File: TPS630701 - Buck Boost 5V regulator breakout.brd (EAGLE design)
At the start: 29.2 x 17.5 mm, 17 parts, among them IC1 TPS630701RNMT

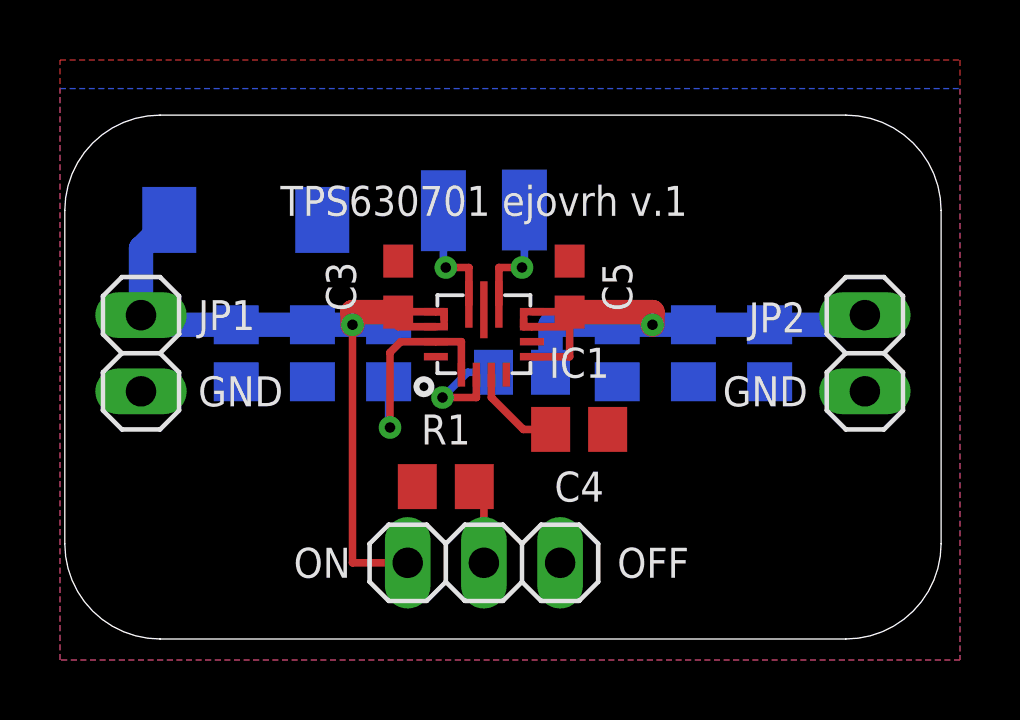
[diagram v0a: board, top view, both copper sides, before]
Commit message: - recreated gerbers with better layer names & corrected mission dimension layer
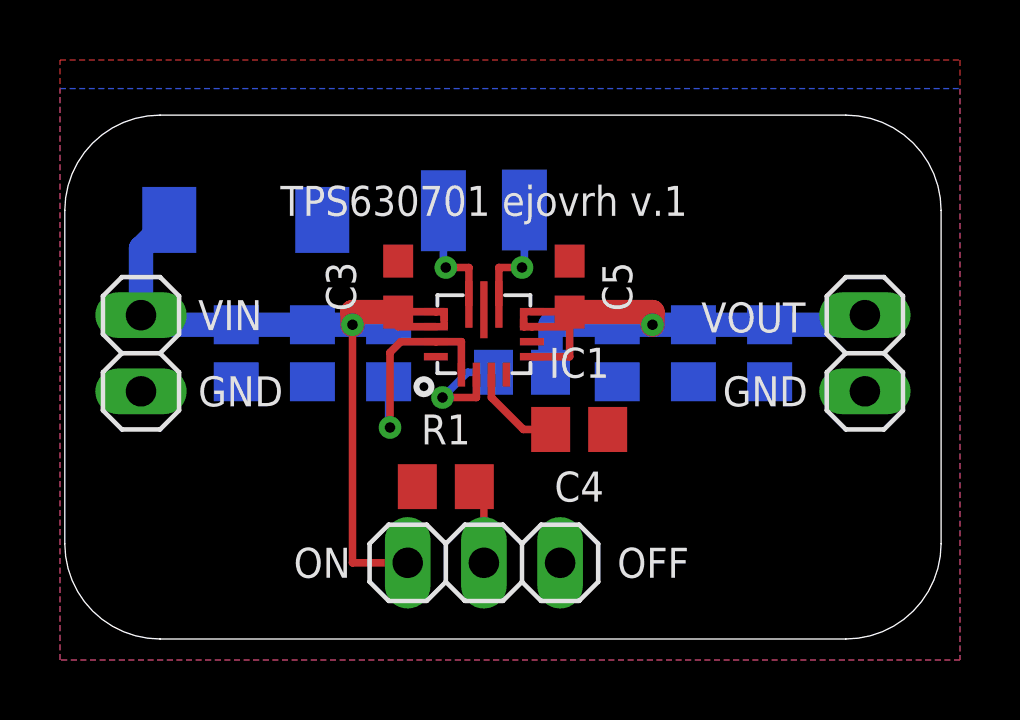
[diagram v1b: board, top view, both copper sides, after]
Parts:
- renumbered JP1 to VIN, JP2 to VOUT
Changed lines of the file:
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@@
 <layer number="14" name="Route14" color="1" fill="6" visible="no" active="no"/>
 <layer number="15" name="Route15" color="4" fill="6" visible="no" active="no"/>
-<layer number="16" name="Bottom" color="1" fill="1" visible="no" active="yes"/>
+<layer number="16" name="Bottom" color="1" fill="1" visible="yes" active="yes"/>
 <layer number="17" name="Pads" color="2" fill="1" visible="yes" active="yes"/>
 <layer number="18" name="Vias" color="2" fill="1" visible="yes" active="yes"/>
@@
 <layer number="20" name="Dimension" color="24" fill="1" visible="yes" active="yes"/>
 <layer number="21" name="tPlace" color="7" fill="1" visible="yes" active="yes"/>
-<layer number="22" name="bPlace" color="7" fill="1" visible="no" active="yes"/>
+<layer number="22" name="bPlace" color="7" fill="1" visible="yes" active="yes"/>
 <layer number="23" name="tOrigins" color="15" fill="1" visible="yes" active="yes"/>
-<layer number="24" name="bOrigins" color="15" fill="1" visible="no" active="yes"/>
+<layer number="24" name="bOrigins" color="15" fill="1" visible="yes" active="yes"/>
 <layer number="25" name="tNames" color="7" fill="1" visible="yes" active="yes"/>
-<layer number="26" name="bNames" color="7" fill="1" visible="no" active="yes"/>
+<layer number="26" name="bNames" color="7" fill="1" visible="yes" active="yes"/>
 <layer number="27" name="tValues" color="7" fill="1" visible="no" active="yes"/>
 <layer number="28" name="bValues" color="7" fill="1" visible="no" active="yes"/>
@@
 <layer number="38" name="bTest" color="7" fill="1" visible="no" active="yes"/>
 <layer number="39" name="tKeepout" color="4" fill="11" visible="yes" active="yes"/>
-<layer number="40" name="bKeepout" color="1" fill="11" visible="no" active="yes"/>
+<layer number="40" name="bKeepout" color="1" fill="11" visible="yes" active="yes"/>
 <layer number="41" name="tRestrict" color="4" fill="10" visible="yes" active="yes"/>
-<layer number="42" name="bRestrict" color="1" fill="10" visible="no" active="yes"/>
-<layer number="43" name="vRestrict" color="2" fill="10" visible="no" active="yes"/>
+<layer number="42" name="bRestrict" color="1" fill="10" visible="yes" active="yes"/>
+<layer number="43" name="vRestrict" color="2" fill="10" visible="yes" active="yes"/>
 <layer number="44" name="Drills" color="7" fill="1" visible="no" active="yes"/>
 <layer number="45" name="Holes" color="7" fill="1" visible="yes" active="yes"/>
@@
 <layer number="50" name="dxf" color="7" fill="1" visible="no" active="no"/>
 <layer number="51" name="tDocu" color="7" fill="1" visible="yes" active="yes"/>
-<layer number="52" name="bDocu" color="7" fill="1" visible="no" active="yes"/>
+<layer number="52" name="bDocu" color="7" fill="1" visible="yes" active="yes"/>
 <layer number="53" name="tGND_GNDA" color="7" fill="9" visible="no" active="no"/>
 <layer number="54" name="bGND_GNDA" color="1" fill="9" visible="no" active="no"/>
@@
 <attribute name="NAME" x="24.13" y="23.8125" size="1" layer="22" font="vector" rot="MR180" align="center"/>
 </element>
-<element name="JP1" library="pinhead" library_urn="urn:adsk.eagle:library:325" package="1X02" package3d_urn="urn:adsk.eagle:package:22435/2" value="Vin" x="12.7" y="22.225" smashed="yes" rot="R90">
+<element name="VIN" library="pinhead" library_urn="urn:adsk.eagle:library:325" package="1X02" package3d_urn="urn:adsk.eagle:package:22435/2" value="Vin" x="12.7" y="22.225" smashed="yes" rot="R90">
 <attribute name="NAME" x="14.605" y="23.495" size="1" layer="25" font="vector" ratio="10" align="center-left"/>
 <attribute name="VALUE" x="15.875" y="19.685" size="1.27" layer="27" rot="R90"/>
 </element>
-<element name="JP2" library="pinhead" library_urn="urn:adsk.eagle:library:325" package="1X02" package3d_urn="urn:adsk.eagle:package:22435/2" value="Vout" x="36.83" y="22.225" smashed="yes" rot="R90">
+<element name="VOUT" library="pinhead" library_urn="urn:adsk.eagle:library:325" package="1X02" package3d_urn="urn:adsk.eagle:package:22435/2" value="Vout" x="36.83" y="22.225" smashed="yes" rot="R90">
 <attribute name="NAME" x="34.8488" y="23.4188" size="1" layer="25" font="vector" ratio="10" align="center-right"/>
 <attribute name="VALUE" x="40.005" y="19.685" size="1.27" layer="27" rot="R90"/>
@@
 <wire x1="22.53" y1="23.11" x2="21.2725" y2="23.11" width="0.254" layer="1"/>
 <wire x1="21.2725" y1="23.11" x2="21.2725" y2="23.5975" width="0.254" layer="1"/>
-<contactref element="JP1" pad="2"/>
+<contactref element="VIN" pad="2"/>
 <wire x1="22.805" y1="23.36" x2="22.805" y2="23.61" width="0.254" layer="1"/>
 <wire x1="22.805" y1="23.61" x2="22.53" y2="23.61" width="0.254" layer="1"/>
@@
 <contactref element="C4" pad="1"/>
 <contactref element="IC1" pad="15-VSEL"/>
-<contactref element="JP2" pad="1"/>
-<contactref element="JP1" pad="1"/>
+<contactref element="VOUT" pad="1"/>
+<contactref element="VIN" pad="1"/>
 <contactref element="JP3" pad="3"/>
 <contactref element="C1" pad="1"/>
@@
 <wire x1="25.73" y1="23.61" x2="26.9875" y2="23.61" width="0.254" layer="1"/>
 <wire x1="26.9875" y1="23.61" x2="26.9875" y2="23.5975" width="0.254" layer="1"/>
-<contactref element="JP2" pad="2"/>
+<contactref element="VOUT" pad="2"/>
 <wire x1="25.455" y1="23.365" x2="25.455" y2="23.11" width="0.254" layer="1"/>
 <wire x1="25.455" y1="23.11" x2="25.73" y2="23.11" width="0.254" layer="1"/>
